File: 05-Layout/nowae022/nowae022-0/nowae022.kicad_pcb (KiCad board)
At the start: 2 copper layers, 80 x 69.3 mm, 0 parts

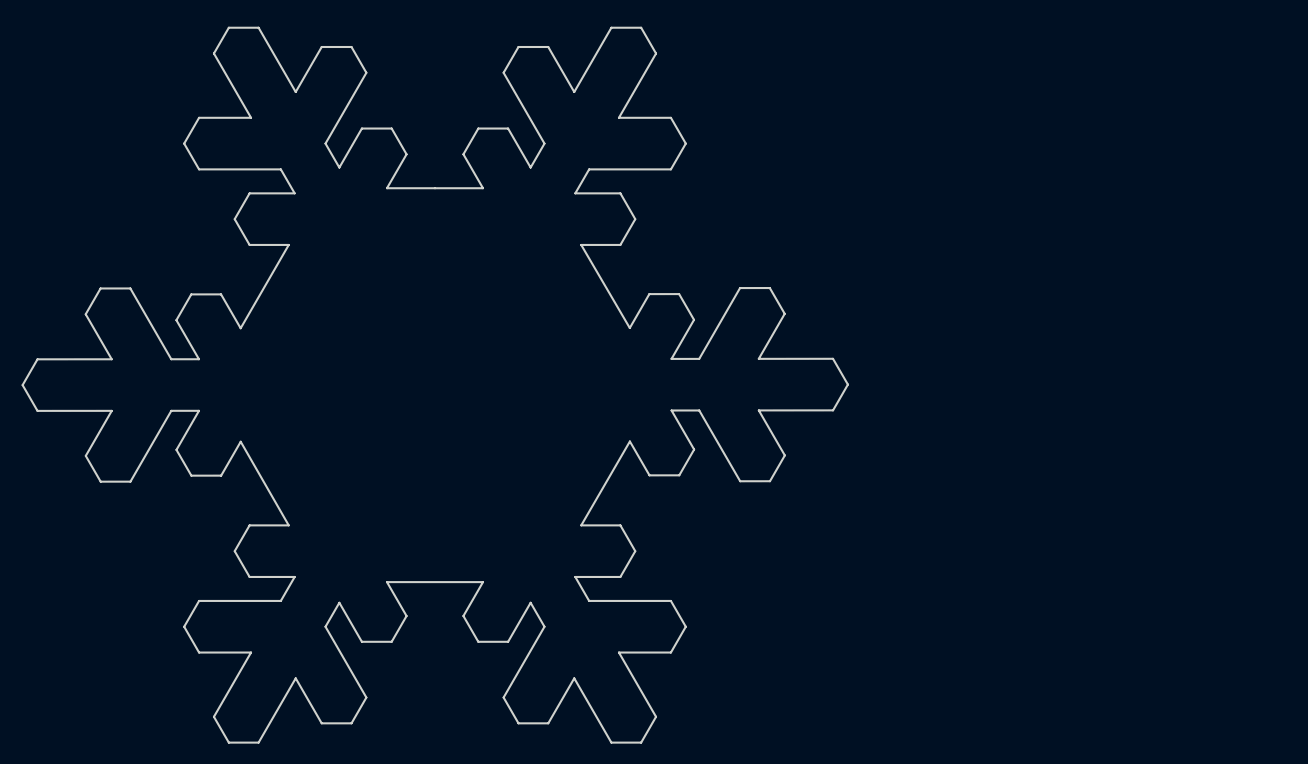
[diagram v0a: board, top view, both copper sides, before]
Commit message: WiP components placement(nowae022-0)
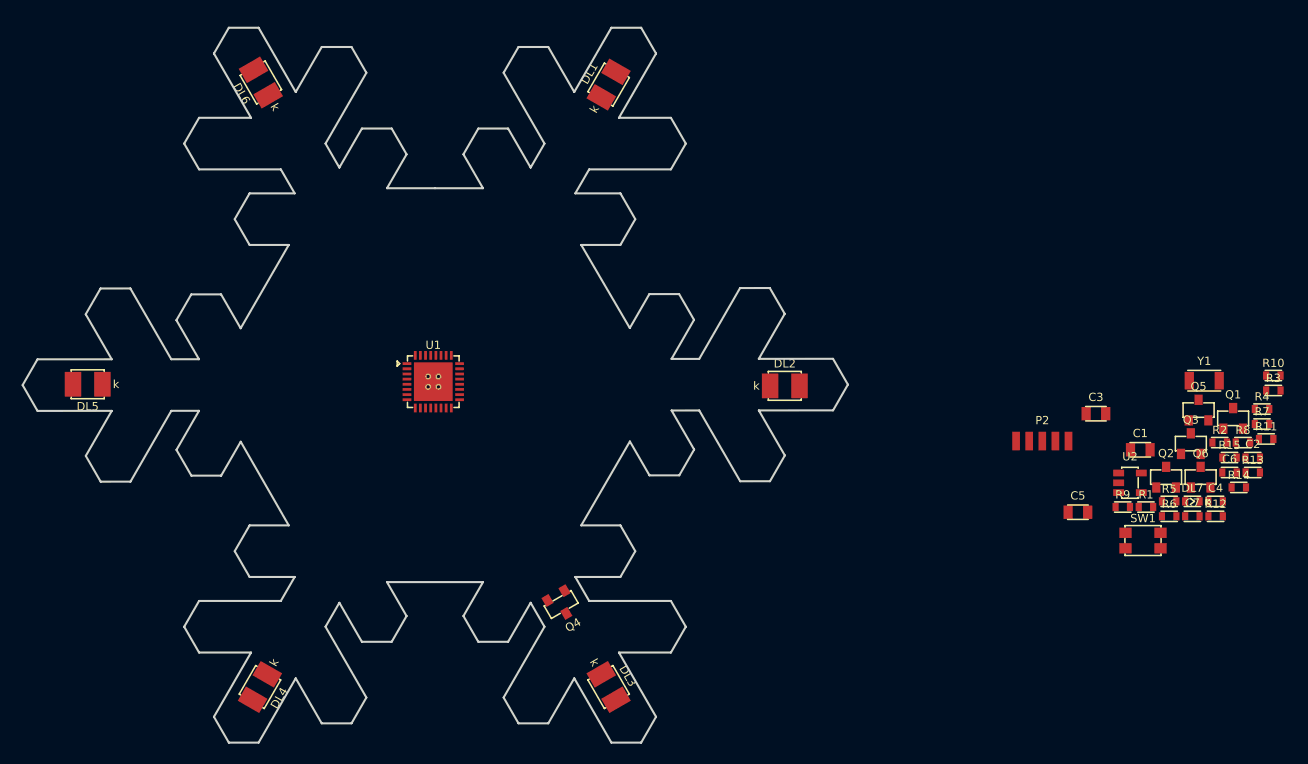
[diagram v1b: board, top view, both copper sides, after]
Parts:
- added C1: 1u, CAPACITOR:CAPACITOR-0805, F.Cu at (208.5, 101.6)
- added C2: 100n, CAPACITOR:CAPACITOR-0603, F.Cu at (219.4, 102.4)
- added C3: 10u, CAPACITOR:CAPACITOR-0805, F.Cu at (204.2, 98.1)
- added C4: 15p, CAPACITOR:CAPACITOR-0603, F.Cu at (215.8, 106.6)
- added C5: 2u2, CAPACITOR:CAPACITOR-0805, F.Cu at (202.5, 107.7)
- added C6: 15p, CAPACITOR:CAPACITOR-0603, F.Cu at (217.2, 103.8)
- added C7: 100n, CAPACITOR:CAPACITOR-0603, F.Cu at (213.6, 108.1)
- added DL1: RED, LEDs:LED-WURTH-WL_SMTW_3528, F.Cu at (157.0, 66.2)
- added DL2: RED, LEDs:LED-WURTH-WL_SMTW_3528, F.Cu at (174.1, 95.4)
- added DL3: RED, LEDs:LED-WURTH-WL_SMTW_3528, F.Cu at (157.0, 124.6)
- added DL4: RED, LEDs:LED-WURTH-WL_SMTW_3528, F.Cu at (123.2, 124.6)
- added DL5: RED, LEDs:LED-WURTH-WL_SMTW_3528, F.Cu at (106.5, 95.2)
- added DL6: RED, LEDs:LED-WURTH-WL_SMTW_3528, F.Cu at (123.3, 66.0)
- added DL7: GREEN, LEDs:LED-0603, F.Cu at (213.6, 106.6)
- added P2: SWD, CONNECTOR:CONN-PAD-5x1-1.27, F.Cu at (199.0, 100.8)
- added Q1: BCW66GLT, SOT:SOT23-3, F.Cu at (217.5, 98.6)
- added Q2: BCW66GLT, SOT:SOT23-3, F.Cu at (211.0, 104.3)
- added Q3: BCW66GLT, SOT:SOT23-3, F.Cu at (213.4, 101.0)
- added Q4: BCW66GLT, SOT:SOT23-3, F.Cu at (152.4, 116.6)
- added Q5: BCW66GLT, SOT:SOT23-3, F.Cu at (214.2, 97.8)
- added Q6: BCW66GLT, SOT:SOT23-3, F.Cu at (214.4, 104.3)
- added R1: 680, RESISTOR:RESISTOR-0603, F.Cu at (209.1, 107.2)
- added R10: 1k2, RESISTOR:RESISTOR-0603, F.Cu at (221.4, 94.4)
- added R11: 1k2, RESISTOR:RESISTOR-0603, F.Cu at (220.7, 100.6)
- added R12: 1k2, RESISTOR:RESISTOR-0603, F.Cu at (215.8, 108.1)
- added R13: 10k, RESISTOR:RESISTOR-0603, F.Cu at (219.4, 103.8)
- added R14: 10k, RESISTOR:RESISTOR-0603, F.Cu at (218.1, 105.3)
- added R15: 270, RESISTOR:RESISTOR-0603, F.Cu at (217.2, 102.4)
- added R2: 680, RESISTOR:RESISTOR-0603, F.Cu at (216.2, 100.9)
- added R3: 680, RESISTOR:RESISTOR-0603, F.Cu at (221.4, 95.9)
- added R4: 680, RESISTOR:RESISTOR-0603, F.Cu at (220.3, 97.7)
- added R5: 680, RESISTOR:RESISTOR-0603, F.Cu at (211.3, 106.6)
- added R6: 680, RESISTOR:RESISTOR-0603, F.Cu at (211.3, 108.1)
- added R7: 1k2, RESISTOR:RESISTOR-0603, F.Cu at (220.3, 99.1)
- added R8: 1k2, RESISTOR:RESISTOR-0603, F.Cu at (218.5, 100.9)
- added R9: 1k2, RESISTOR:RESISTOR-0603, F.Cu at (206.8, 107.2)
- added SW1: BUTTON-WE_434153017835, BUTTON:BUTTON-WE-434153017835, F.Cu at (208.8, 110.4)
- added U1: MKL15Z128VFM4, QFN:QFN32_5x5_0.5_32+1, F.Cu at (140.0, 95.0)
- added U2: TPS70933DBV, SOT:SOT23-5, F.Cu at (207.5, 104.8)
- added Y1: 32768, CRYSTAL:CRYSTAL-1206, F.Cu at (214.7, 94.9)

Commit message: WiP components placement and routing (nowae022-0)
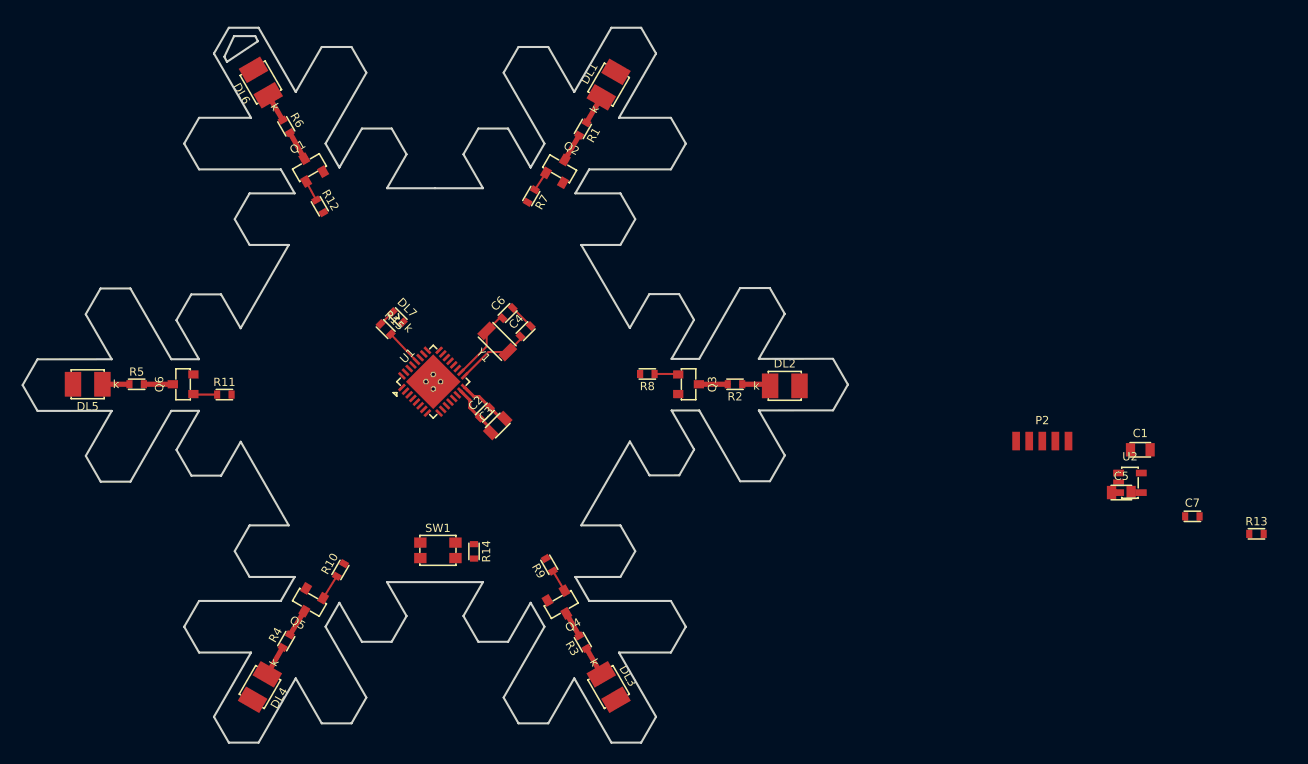
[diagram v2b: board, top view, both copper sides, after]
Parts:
- moved R11 101.1 mm to (119.8, 96.2)
- moved R5 100.7 mm to (111.2, 95.2)
- moved Q6 99.0 mm to (115.8, 95.2), turned to 90 degrees
- moved R4 97.2 mm to (125.8, 120.2), turned to 60 degrees
- moved R6 93.6 mm to (125.8, 70.2), turned to 300 degrees
- moved Q1 92.8 mm to (128.0, 74.2), turned to 30 degrees
- moved R10 92.4 mm to (131.0, 113.2), turned to 60 degrees
- moved R12 91.9 mm to (129.0, 78.0), turned to 300 degrees
- moved Q5 88.2 mm to (128.0, 116.4), turned to 150 degrees
- moved R15 82.7 mm to (135.4, 89.9), turned to 315 degrees
- moved DL7 79.1 mm to (136.6, 88.8), turned to 315 degrees
- moved C2 74.6 mm to (145.0, 98.0), turned to 45 degrees
- moved R14 74.4 mm to (143.9, 111.5), turned to 270 degrees
- moved R7 74.2 mm to (149.5, 77.0), turned to 240 degrees
- moved C6 71.7 mm to (147.2, 88.3), turned to 45 degrees
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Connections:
- DL1 pad 2: Net-(DL1-Pad2) -> +VIN
- DL2 pad 2: Net-(DL2-Pad2) -> +VIN
- DL3 pad 2: Net-(DL3-Pad2) -> +VIN
- DL4 pad 2: Net-(DL4-Pad2) -> +VIN
- DL5 pad 2: Net-(DL5-Pad2) -> +VIN
- DL6 pad 2: Net-(DL6-Pad2) -> +VIN
- Q1 pad 3: Net-(DL6-Pad1) -> Net-(Q1-Pad3)
- Q2 pad 3: Net-(DL1-Pad1) -> Net-(Q2-Pad3)
- Q3 pad 3: Net-(DL2-Pad1) -> Net-(Q3-Pad3)
- Q4 pad 3: Net-(DL3-Pad1) -> Net-(Q4-Pad3)
- Q5 pad 3: Net-(DL4-Pad1) -> Net-(Q5-Pad3)
- Q6 pad 3: Net-(DL5-Pad1) -> Net-(Q6-Pad3)
- R1 pad 1: +VIN -> Net-(DL1-Pad1)
- R1 pad 2: Net-(DL1-Pad2) -> Net-(Q2-Pad3)
- R2 pad 1: +VIN -> Net-(DL2-Pad1)
- R2 pad 2: Net-(DL2-Pad2) -> Net-(Q3-Pad3)
- R3 pad 1: +VIN -> Net-(DL3-Pad1)
- R3 pad 2: Net-(DL3-Pad2) -> Net-(Q4-Pad3)
- R4 pad 1: +VIN -> Net-(DL4-Pad1)
- R4 pad 2: Net-(DL4-Pad2) -> Net-(Q5-Pad3)
- R5 pad 1: +VIN -> Net-(DL5-Pad1)
- R5 pad 2: Net-(DL5-Pad2) -> Net-(Q6-Pad3)
- R6 pad 1: +VIN -> Net-(DL6-Pad1)
- R6 pad 2: Net-(DL6-Pad2) -> Net-(Q1-Pad3)
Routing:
- net GND: track 0.00 -> 7.61 mm
- net Net-(C4-Pad1): track 0.00 -> 7.18 mm
- net Net-(C6-Pad1): track 0.00 -> 7.08 mm
- net +3.3V: track 0.00 -> 5.20 mm
- net /MCU_STATUS: track 0.00 -> 3.62 mm
- net Net-(DL4-Pad1): track 0.00 -> 3.00 mm
- net Net-(DL3-Pad1): track 0.00 -> 2.89 mm
- net Net-(Q1-Pad3): track 0.00 -> 2.89 mm
- net Net-(DL1-Pad1): track 0.00 -> 2.85 mm
- net Net-(Q3-Pad3): track 0.00 -> 2.80 mm
- net Net-(Q6-Pad3): track 0.00 -> 2.80 mm
- net Net-(DL6-Pad1): track 0.00 -> 2.79 mm
- net Net-(Q2-Pad3): track 0.00 -> 2.77 mm
- net Net-(DL2-Pad1): track 0.00 -> 2.76 mm
- net Net-(Q5-Pad3): track 0.00 -> 2.69 mm
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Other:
- outline, holes or cut-outs redrawn
- net class Default: trace_width 0.25 -> 0.2; via_dia 0.8 -> 0.6; via_drill 0.4 -> 0.3

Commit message: WiP routing (nowae022-0)
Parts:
- added P1: SUPPLY, CONNECTOR_MKDS:CONN-MKDS1_2-3.81, B.Cu at (140.2, 82.2)
- P2: footprint CONNECTOR:CONN-PAD-5x1-1.27 -> CONNECTOR:CONN-STRIP-5x1-2.54
- moved C1 75.7 mm to (136.5, 78.2), turned to 270 degrees
- moved R13 73.9 mm to (146.0, 105.8), turned to 180 degrees
- moved U2 72.3 mm to (140.2, 78.2)
- moved C5 68.7 mm to (143.8, 78.2), turned to 270 degrees
- moved C7 67.5 mm to (146.1, 107.4)
- moved P2 59.5 mm to (140.2, 109.9)
- moved R14 18.5 mm to (132.8, 96.8), turned to 45 degrees
- moved SW1 13.2 mm to (135.2, 99.2), turned to 135 degrees
- moved DL7 1.77 mm to (137.8, 87.5)
- moved R15 1.77 mm to (136.6, 88.7)
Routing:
- net +VIN: track 0.00 -> 218.9 mm, vias 0 -> 6
- net +3.3V: track 5.20 -> 67.0 mm, vias 0 -> 1
- net /BALL_LED3: track 0.00 -> 38.6 mm, vias 0 -> 2
- net /RESET: track 0.00 -> 35.1 mm, vias 0 -> 2
- net /BALL_LED4: track 0.00 -> 29.3 mm, vias 0 -> 2
- net /BALL_LED2: track 0.00 -> 26.8 mm, vias 0 -> 2
- net /BALL_LED5: track 0.00 -> 25.3 mm, vias 0 -> 2
- net /BALL_LED6: track 0.00 -> 18.6 mm
- net /BALL_LED1: track 0.00 -> 18.3 mm
- net /MCU_PROG: track 0.00 -> 14.4 mm, vias 0 -> 2
- net /SWCLK: track 0.00 -> 14.2 mm
- net /SWDIO: track 0.00 -> 13.6 mm
- net GND: track 7.61 -> 20.7 mm
- net /MCU_STATUS: track 3.62 -> 4.68 mm
- added copper zone on F.Cu, net +VIN
- added copper zone on F.Cu, net GND

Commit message: Routing ended (nowae022-0)
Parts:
- added G***: LOGO, LOGO:LOGO_NOWAE_25MM_FSILK, B.Cu at (140.0, 97.5)
- added G***: LOGO, EXTLOGO:LOGO_CC-BY-SA_10MM_FSILK, B.Cu at (134.3, 104.2)
- added G***: LOGO, EXTLOGO:LOGO_OSH_5MM_FSILK, B.Cu at (147.3, 104.1)
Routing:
- net +3.3V: track 67.0 -> 92.2 mm, vias 1 -> 3
- net GND: track 20.7 -> 36.3 mm, vias 0 -> 10
- net +VIN: track 218.9 -> 216.0 mm
- net /RESET: track 35.1 -> 33.3 mm
- added copper zone on B.Cu, net GND
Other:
- board text added: "Christmas Tree ball #1 NOWAE022-0"
- board text added: "designed by"

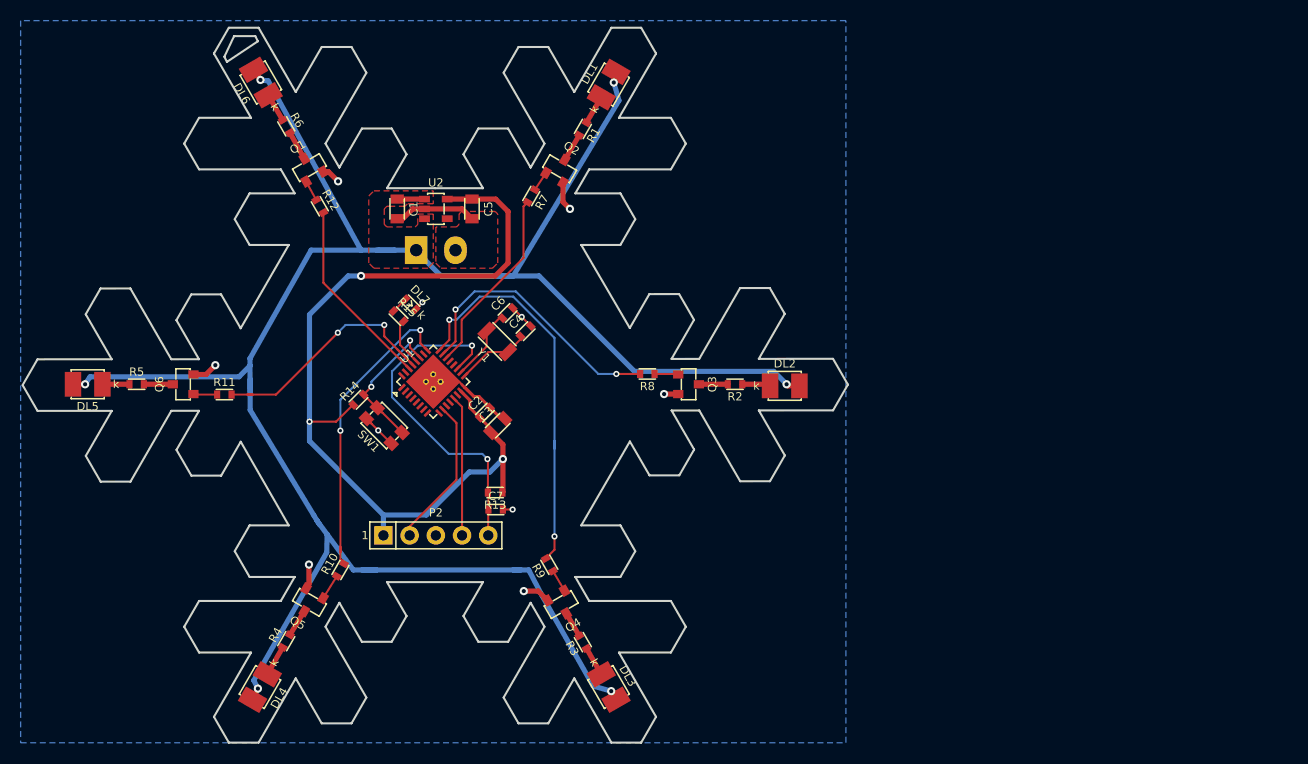
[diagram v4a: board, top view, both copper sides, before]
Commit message: Fixed components silkscreen and fab (nowae022-0)
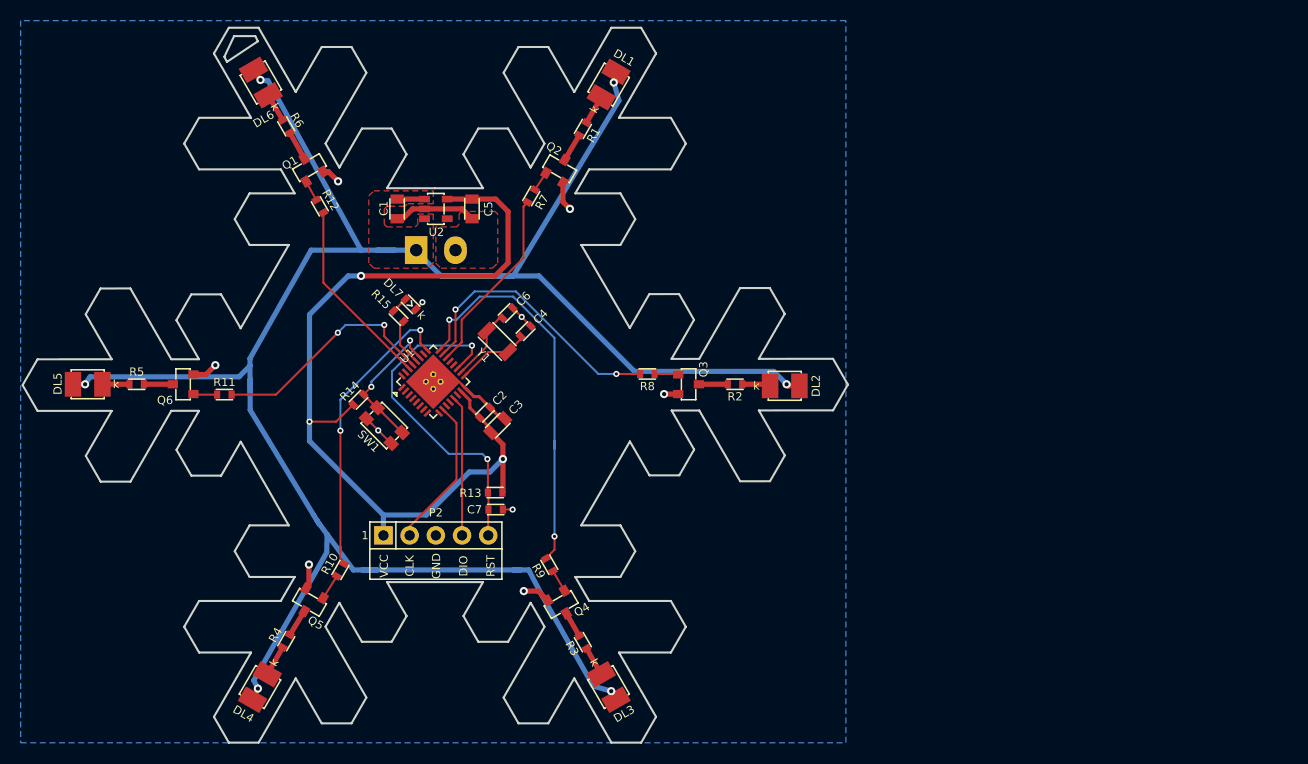
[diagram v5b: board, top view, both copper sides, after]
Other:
- board text added: "CLK"
- board text added: "DIO"
- board text added: "GND"
- board text added: "RST"
- board text added: "VCC"

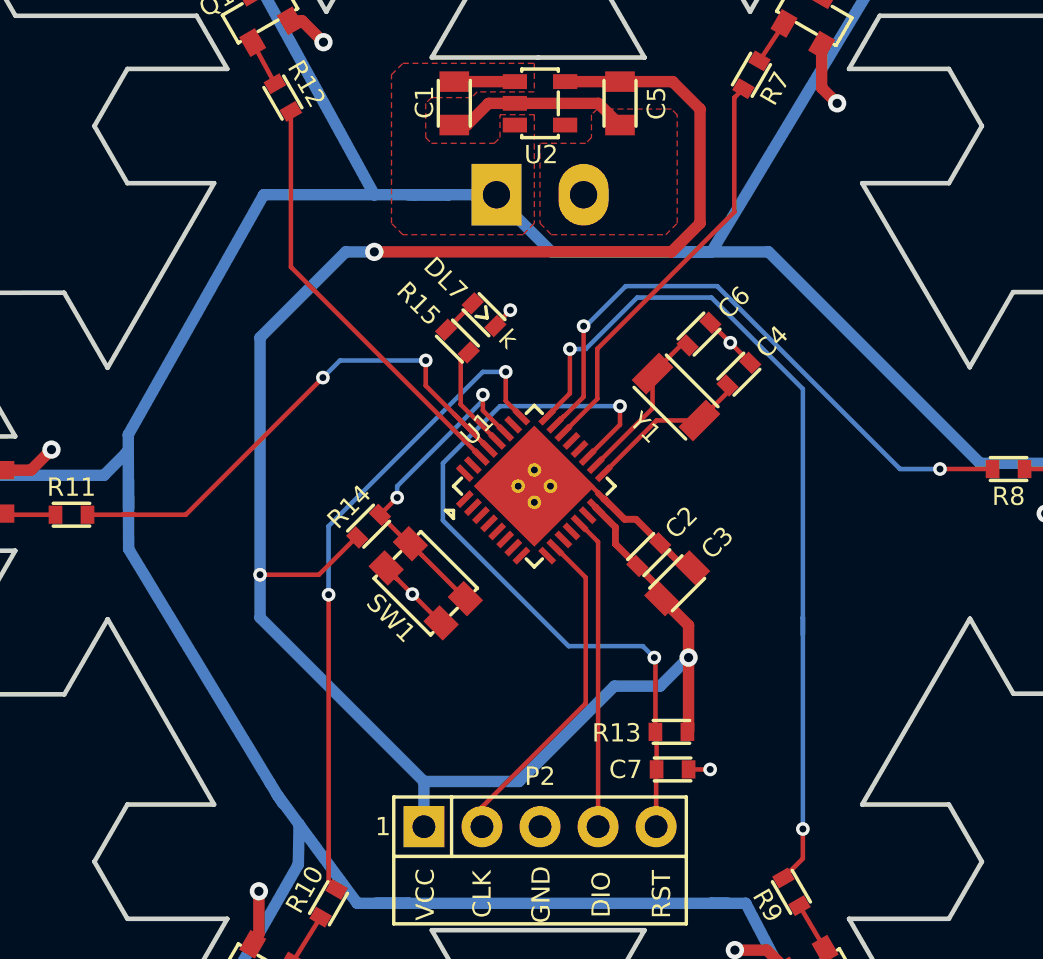
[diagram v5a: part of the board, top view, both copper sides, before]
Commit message: Added some snowflake picture on silkscreen (nowae022-0)
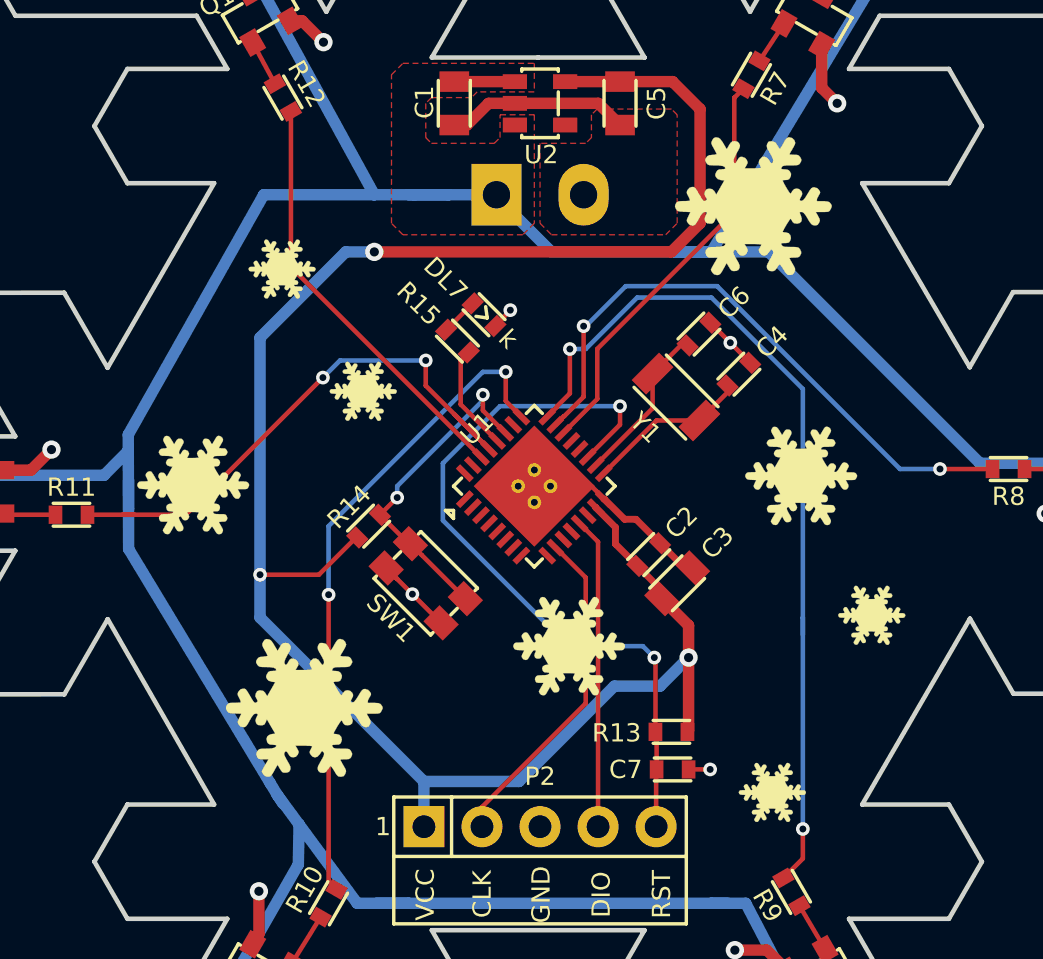
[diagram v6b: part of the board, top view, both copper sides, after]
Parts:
- added G***: LOGO, EXTLOGO:LOGO_SNOW1_3MM_FSILK, F.Cu at (154.8, 100.7)
- added G***: LOGO, EXTLOGO:LOGO_SNOW1_3MM_FSILK, F.Cu at (150.4, 108.4)
- added G***: LOGO, EXTLOGO:LOGO_SNOW1_5MM_FSILK, F.Cu at (141.5, 102.0)
- added G***: LOGO, EXTLOGO:LOGO_SNOW1_5MM_FSILK, F.Cu at (125.0, 95.0)
- added G***: LOGO, EXTLOGO:LOGO_SNOW1_7MM_FSILK, F.Cu at (149.6, 82.8)
- added G***: LOGO, EXTLOGO:LOGO_SNOW1_7MM_FSILK, F.Cu at (129.9, 104.7)
- added G***: LOGO, EXTLOGO:LOGO_SNOW1_5MM_FSILK, F.Cu at (151.7, 94.5)
- added G***: LOGO, EXTLOGO:LOGO_SNOW1_3MM_FSILK, F.Cu at (128.9, 85.5)
- added G***: LOGO, EXTLOGO:LOGO_SNOW1_3MM_FSILK, F.Cu at (132.5, 90.8)
